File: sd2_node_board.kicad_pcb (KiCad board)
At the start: 4 copper layers, 100.4 x 83.9 mm, 45 parts, among them J1 CON-SOCJ-2155, J2 USB_B_Micro, J3 S1, J4 S2, J5 Indicator, J6 S3, J7 JTAG, J8 S4, Q1 MBT3904DW1, SW1 SW_Push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

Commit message: Finish placing components
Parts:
- moved SW1 155.5 mm to (153.7, 136.4), turned to -90 degrees
- moved R2 129.1 mm to (107.1, 146.4), turned to 180 degrees
- moved R1 126.3 mm to (120.1, 121.2), turned to 90 degrees
- moved D1 120.3 mm to (107.2, 142.0), turned to 180 degrees
- moved D2 113.3 mm to (161.5, 138.2)
- moved R3 113.2 mm to (103.1, 87.4), turned to 180 degrees
- moved R5 112.4 mm to (161.3, 133.3)
- moved R4 106.9 mm to (103.1, 91.4), turned to 180 degrees
- moved C1 100.7 mm to (103.1, 83.8)
- moved U2 99.2 mm to (137.2, 105.9)
- moved C2 99.0 mm to (97.8, 84.8), turned to 90 degrees
- moved C3 98.8 mm to (97.8, 90.4), turned to -90 degrees
- moved J7 96.2 mm to (153.7, 124.5), turned to 180 degrees
- moved R6 93.4 mm to (113.2, 125.2), turned to 180 degrees
- moved Q1 90.9 mm to (113.2, 120.7)
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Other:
- board size 100.4 x 83.9 mm -> 93.3 x 83.9 mm

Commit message: Finish routing
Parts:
- moved R5 58.4 mm to (104.1, 145.5)
- moved D2 58.4 mm to (104.1, 149.1)
- moved J7 11.7 mm to (142.5, 121.2), turned to -90 degrees
- moved D1 7.83 mm to (109.6, 149.4), turned to 0 degrees
- moved SW1 7.05 mm to (157.2, 142.5), turned to 180 degrees
- moved R11 3.24 mm to (141.2, 83.1)
- moved R2 2.95 mm to (109.7, 145.0), turned to 0 degrees
- moved C12 2.91 mm to (146.1, 82.8)
- moved C14 2.76 mm to (154.9, 82.8)
- moved C11 2.76 mm to (150.6, 82.8)
- moved R12 2.73 mm to (159.0, 83.0)
- moved C8 1.97 mm to (133.9, 79.5)
- moved R9 1.70 mm to (130.3, 87.4)
- moved C9 1.47 mm to (118.4, 87.4)
- moved L1 1.29 mm to (118.4, 80.5)
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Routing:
- net +3.3V: track 0.00 -> 230.6 mm, vias 0 -> 4
- net +5V: track 0.00 -> 226.6 mm, vias 0 -> 1
- net GND: track 0.00 -> 211.3 mm, vias 0 -> 12
- net IND_CS: track 0.00 -> 106.1 mm, vias 0 -> 1
- net VIN: track 0.00 -> 101.8 mm, vias 0 -> 4
- net IND_CLK: track 0.00 -> 92.6 mm, vias 0 -> 1
- net IND_DIN: track 0.00 -> 86.6 mm, vias 0 -> 1
- net CHIP_PU: track 0.00 -> 77.9 mm, vias 0 -> 2
- net TRIG3: track 0.00 -> 76.5 mm, vias 0 -> 1
- net S3_ECHO_B: track 0.00 -> 66.6 mm, vias 0 -> 1
- net TRIG2: track 0.00 -> 66.4 mm, vias 0 -> 1
- net RTS_XBEE: track 0.00 -> 64.7 mm
- net S3_ECHO_A: track 0.00 -> 64.6 mm, vias 0 -> 1
- net S2_ECHO_B: track 0.00 -> 64.2 mm
- net S1_ECHO_A: track 0.00 -> 59.3 mm, vias 0 -> 1
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- added copper zone on In2.Cu, net GND

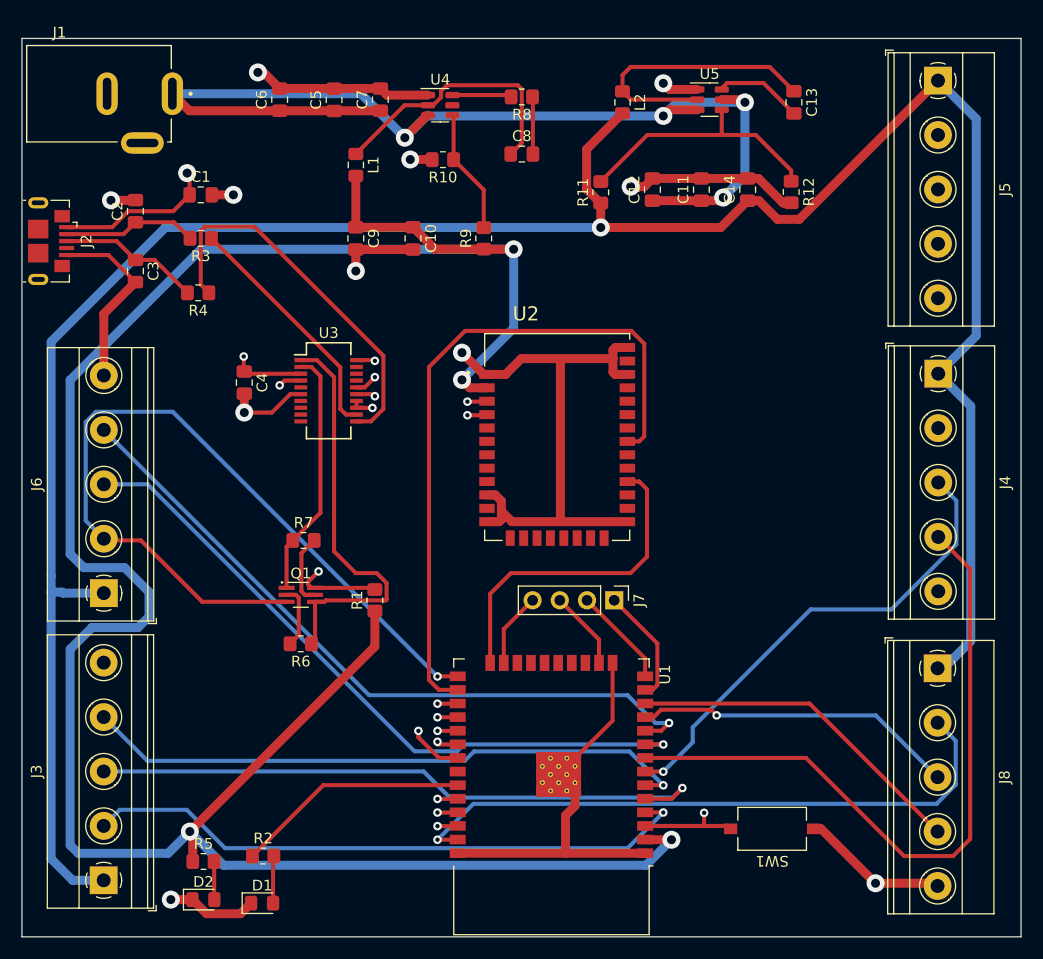
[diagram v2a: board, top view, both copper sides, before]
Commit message: Finish silkscreen and fix thermal pad
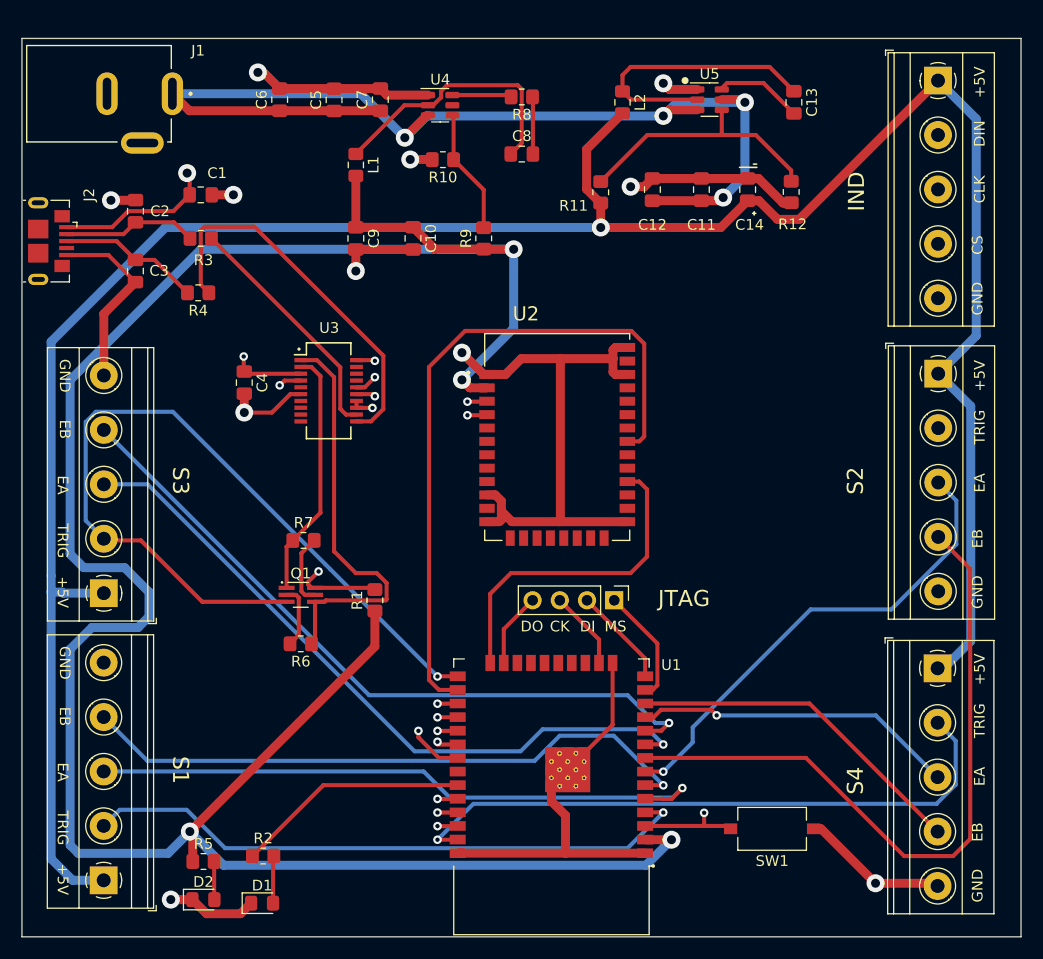
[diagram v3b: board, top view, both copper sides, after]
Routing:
- net S1_ECHO_B: track 57.3 -> 58.5 mm
- net S3_ECHO_A: track 64.6 -> 65.7 mm
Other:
- board text added: "+5V"
- board text added: "CK"
- board text added: "CLK"
- board text added: "CS"
- board text added: "DI"
- board text added: "DIN"
- board text added: "DO"
- board text added: "EA"
- board text added: "EB"
- board text added: "GND"
- board text added: "IND"
- board text added: "JTAG"
- board text added: "MS"
- board text added: "S1"
- board text added: "S2"
- board text added: "S3"
- board text added: "S4"
- board text added: "TRIG"
- board text added: "UCF ECE Senior Design Group 14 FastCpE Rev 1.0"

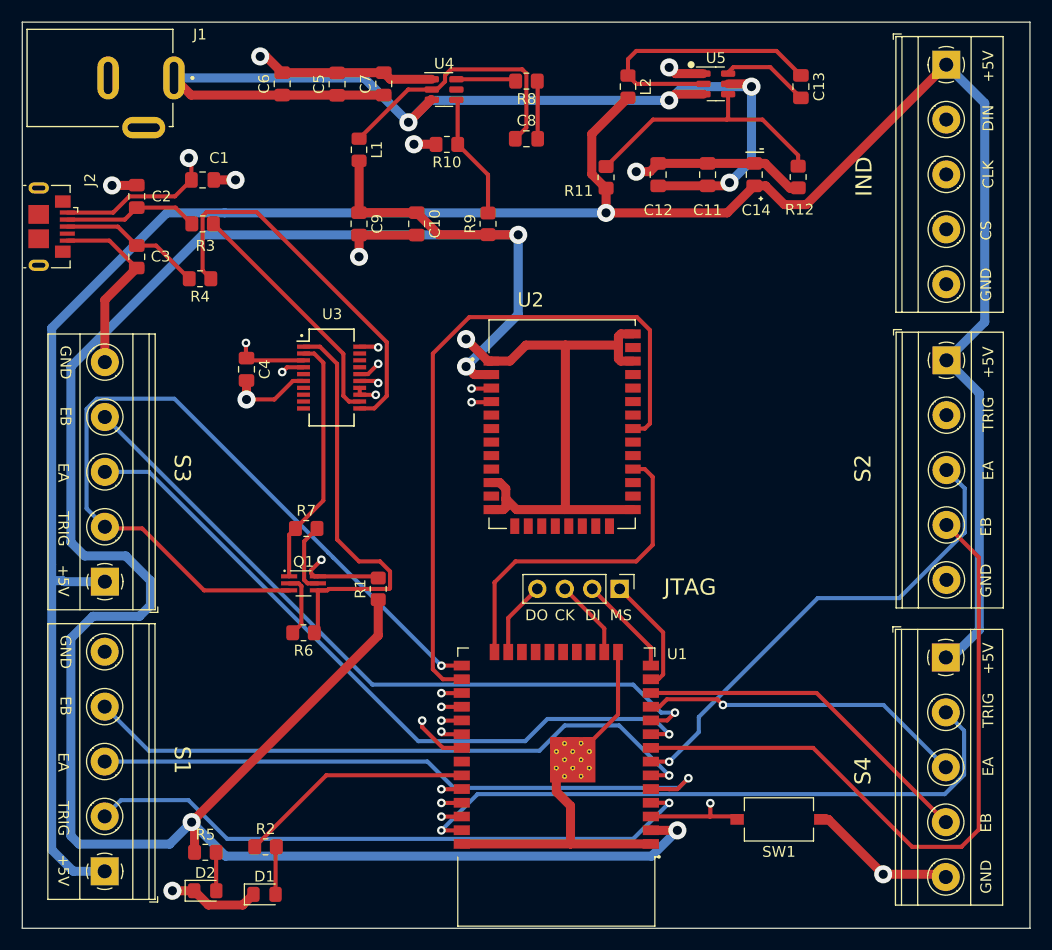
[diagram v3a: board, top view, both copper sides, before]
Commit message: Fix silkscreen and generate Gerbers
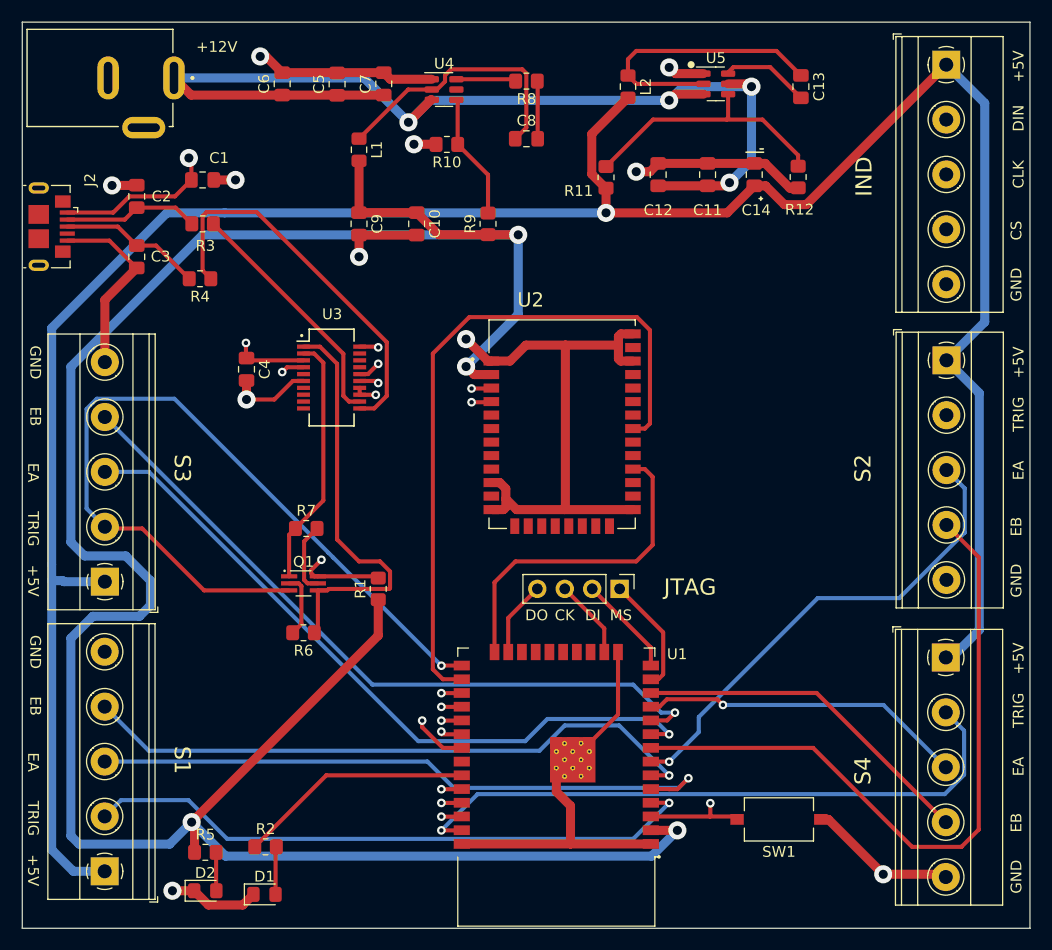
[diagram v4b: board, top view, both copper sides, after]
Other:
- board text added: "+12V"
